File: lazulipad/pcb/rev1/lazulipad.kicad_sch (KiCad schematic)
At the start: 93 parts

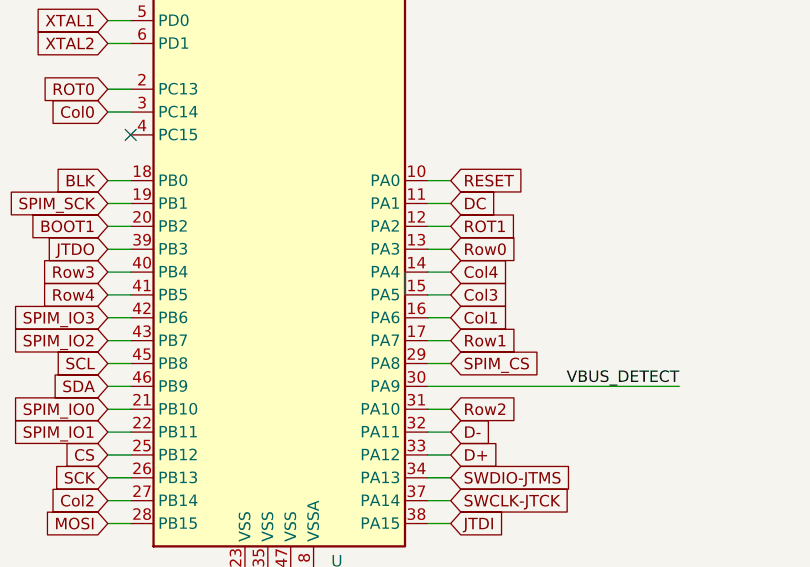
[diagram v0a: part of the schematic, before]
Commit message: Update paws60 hotswap socket footprint and lazulipad
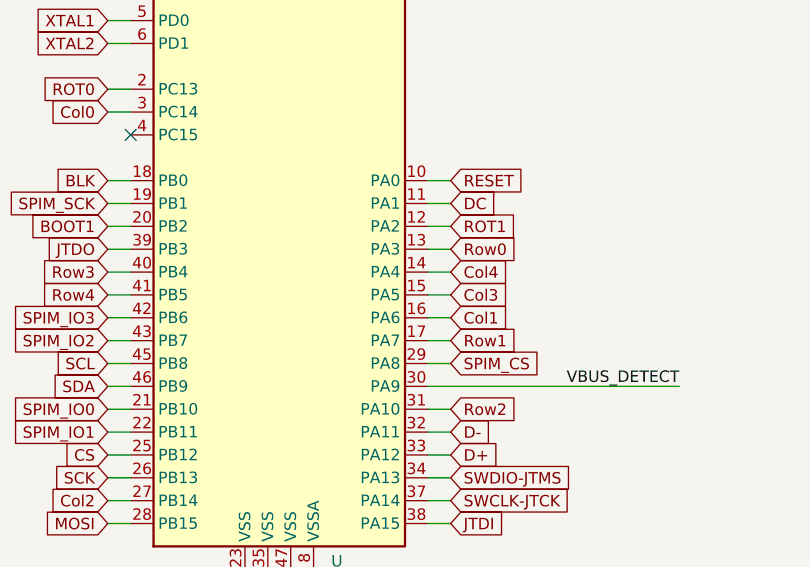
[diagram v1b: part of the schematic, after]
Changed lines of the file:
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@@
-    (stroke (width 0) (type default))
-  )
-  (wire (pts (xy 63.5 92.71) (xy 63.5 90.17))
     (stroke (width 0) (type default))
   )
